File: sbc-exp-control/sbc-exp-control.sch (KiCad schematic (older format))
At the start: 10 parts, among them J1 P, SW1 U, SW2 D, SW3 L, SW4 R, SW5 A, SW6 B, SW7 C

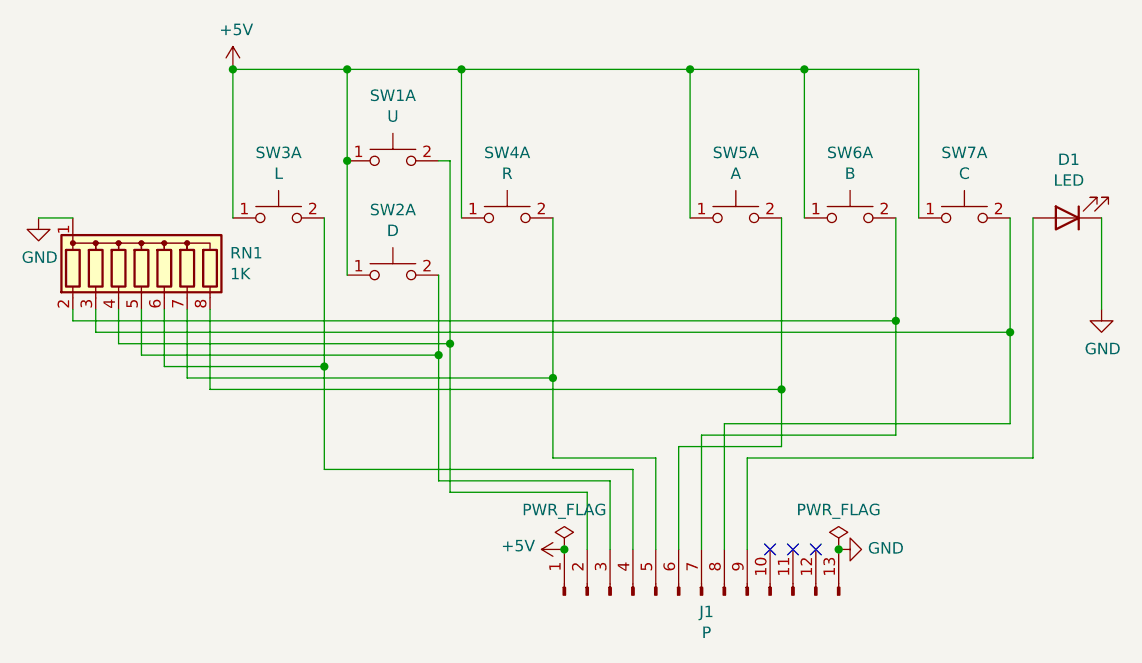
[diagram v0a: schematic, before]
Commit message: SBC Controller: Fix v1.0 errata
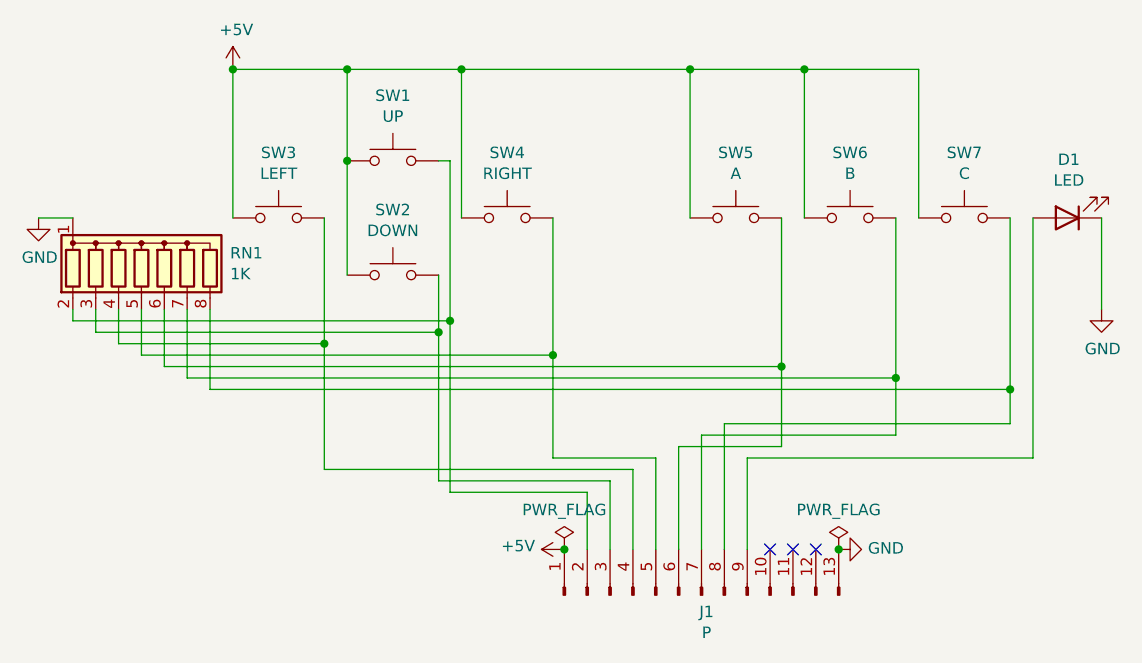
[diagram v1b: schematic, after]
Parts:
- removed SW1: U, switch:SW_TH_Tactile_Omron_B3F-10xx, symbol switch:SW_Push_Dual_x2
- removed SW2: D, switch:SW_TH_Tactile_Omron_B3F-10xx, symbol switch:SW_Push_Dual_x2
- removed SW3: L, switch:SW_TH_Tactile_Omron_B3F-10xx, symbol switch:SW_Push_Dual_x2
- removed SW4: R, switch:SW_TH_Tactile_Omron_B3F-10xx, symbol switch:SW_Push_Dual_x2
- removed SW5: A, switch:SW_TH_Tactile_Omron_B3F-10xx, symbol switch:SW_Push_Dual_x2
- removed SW6: B, switch:SW_TH_Tactile_Omron_B3F-10xx, symbol switch:SW_Push_Dual_x2
- removed SW7: C, switch:SW_TH_Tactile_Omron_B3F-10xx, symbol switch:SW_Push_Dual_x2
- added SW1: UP, switch:SW_TH_Tactile_Omron_B3F-10xx, symbol switch_tactile:SW_Tactile_Push
- added SW2: DOWN, switch:SW_TH_Tactile_Omron_B3F-10xx, symbol switch_tactile:SW_Tactile_Push
- added SW3: LEFT, switch:SW_TH_Tactile_Omron_B3F-10xx, symbol switch_tactile:SW_Tactile_Push
- added SW4: RIGHT, switch:SW_TH_Tactile_Omron_B3F-10xx, symbol switch_tactile:SW_Tactile_Push
- added SW5: A, switch:SW_TH_Tactile_Omron_B3F-10xx, symbol switch_tactile:SW_Tactile_Push
- added SW6: B, switch:SW_TH_Tactile_Omron_B3F-10xx, symbol switch_tactile:SW_Tactile_Push
- added SW7: C, switch:SW_TH_Tactile_Omron_B3F-10xx, symbol switch_tactile:SW_Tactile_Push
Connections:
- net +5V: now also SW1.1, SW2.1, SW3.1, SW4.1, SW5.1, SW6.1, SW7.1
- net at RN1.2 (R1): now also J1.2 (Pin_2), SW1.3; no longer J1.7 (Pin_7)
- net at RN1.3 (R2): now also J1.3 (Pin_3), SW2.3; no longer J1.8 (Pin_8)
- net at RN1.4 (R3): now also J1.4 (Pin_4), SW3.3; no longer J1.2 (Pin_2)
- net at RN1.5 (R4): now also J1.5 (Pin_5), SW4.3; no longer J1.3 (Pin_3)
- net at RN1.6 (R5): now also J1.6 (Pin_6), SW5.3; no longer J1.4 (Pin_4)
- net at RN1.7 (R6): now also J1.7 (Pin_7), SW6.3; no longer J1.5 (Pin_5)
- net at RN1.8 (R7): now also J1.8 (Pin_8), SW7.3; no longer J1.6 (Pin_6)
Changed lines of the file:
@@
 Sheet 1 1
 Title "6502 SBC Expansion - Controller"
-Date "2021-09-15"
-Rev "1.0"
+Date "2021-10-03"
+Rev "1.1"
 Comp ""
 Comment1 ""
@@
 	1    0    0    -1
 $EndComp
-$Comp
-L switch:SW_Push_Dual_x2 SW1
-U 1 1 6149A8C0
-P 4400 2900
-F 0 "SW1" H 4400 3185 50  0000 C CNN
-F 1 "U" H 4400 3094 50  0000 C CNN
-F 2 "switch:SW_TH_Tactile_Omron_B3F-10xx" H 4400 3100 50  0001 C CNN
-F 3 "~" H 4400 3100 50  0001 C CNN
-	1    4400 2900
-	1    0    0    -1
-$EndComp
-$Comp
-L switch:SW_Push_Dual_x2 SW2
-U 1 1 6149E1BC
-P 4400 3400
-F 0 "SW2" H 4400 3685 50  0000 C CNN
-F 1 "D" H 4400 3594 50  0000 C CNN
-F 2 "switch:SW_TH_Tactile_Omron_B3F-10xx" H 4400 3600 50  0001 C CNN
-F 3 "~" H 4400 3600 50  0001 C CNN
-	1    4400 3400
-	1    0    0    -1
-$EndComp
-$Comp
-L switch:SW_Push_Dual_x2 SW3
-U 1 1 6149E449
-P 3900 3150
-F 0 "SW3" H 3900 3435 50  0000 C CNN
-F 1 "L" H 3900 3344 50  0000 C CNN
-F 2 "switch:SW_TH_Tactile_Omron_B3F-10xx" H 3900 3350 50  0001 C CNN
-F 3 "~" H 3900 3350 50  0001 C CNN
-	1    3900 3150
-	1    0    0    -1
-$EndComp
-$Comp
-L switch:SW_Push_Dual_x2 SW4
-U 1 1 6149E6A4
-P 4900 3150
-F 0 "SW4" H 4900 3435 50  0000 C CNN
-F 1 "R" H 4900 3344 50  0000 C CNN
-F 2 "switch:SW_TH_Tactile_Omron_B3F-10xx" H 4900 3350 50  0001 C CNN
-F 3 "~" H 4900 3350 50  0001 C CNN
-	1    4900 3150
-	1    0    0    -1
-$EndComp
-$Comp
-L switch:SW_Push_Dual_x2 SW5
-U 1 1 6149E910
-P 5900 3150
-F 0 "SW5" H 5900 3435 50  0000 C CNN
-F 1 "A" H 5900 3344 50  0000 C CNN
-F 2 "switch:SW_TH_Tactile_Omron_B3F-10xx" H 5900 3350 50  0001 C CNN
-F 3 "~" H 5900 3350 50  0001 C CNN
-	1    5900 3150
-	1    0    0    -1
-$EndComp
-$Comp
-L switch:SW_Push_Dual_x2 SW6
-U 1 1 6149ECA4
-P 6400 3150
-F 0 "SW6" H 6400 3435 50  0000 C CNN
-F 1 "B" H 6400 3344 50  0000 C CNN
-F 2 "switch:SW_TH_Tactile_Omron_B3F-10xx" H 6400 3350 50  0001 C CNN
-F 3 "~" H 6400 3350 50  0001 C CNN
-	1    6400 3150
-	1    0    0    -1
-$EndComp
-$Comp
-L switch:SW_Push_Dual_x2 SW7
-U 1 1 6149EF8F
-P 6900 3150
-F 0 "SW7" H 6900 3435 50  0000 C CNN
-F 1 "C" H 6900 3344 50  0000 C CNN
-F 2 "switch:SW_TH_Tactile_Omron_B3F-10xx" H 6900 3350 50  0001 C CNN
-F 3 "~" H 6900 3350 50  0001 C CNN
-	1    6900 3150
-	1    0    0    -1
-$EndComp
 Wire Wire Line
 	4600 2900 4650 2900
-Wire Wire Line
-	4650 2900 4650 3700
-Wire Wire Line
-	4100 4250 4100 3800
-Wire Wire Line
-	5100 4200 5100 3850
-Wire Wire Line
-	6100 4150 6100 3900
 Wire Wire Line
 	3700 3150 3700 2500
@@
 Wire Wire Line
 	4700 2500 5700 2500
-Wire Wire Line
-	4200 2900 4200 2500
 Connection ~ 4200 2500
 Wire Wire Line
 	4200 2500 4700 2500
-Wire Wire Line
-	4200 3400 4200 2900
-Connection ~ 4200 2900
 $Comp
 L power:+5V #PWR0101
@@
 	3000 3550 3000 3600
 Wire Wire Line
-	3000 3600 6600 3600
-Wire Wire Line
-	6600 4100 6600 3600
-Wire Wire Line
-	6600 3600 6600 3150
-Connection ~ 6600 3600
-Wire Wire Line
 	3100 3550 3100 3650
 Wire Wire Line
-	3100 3650 7100 3650
-Wire Wire Line
-	7100 4050 7100 3650
-Wire Wire Line
-	7100 3650 7100 3150
-Connection ~ 7100 3650
-Wire Wire Line
-	4600 4300 4600 3750
-Wire Wire Line
 	3200 3550 3200 3700
 Wire Wire Line
-	3200 3700 4650 3700
-Connection ~ 4650 3700
-Wire Wire Line
-	4650 3700 4650 4350
-Wire Wire Line
 	3300 3550 3300 3750
 Wire Wire Line
-	3300 3750 4600 3750
-Connection ~ 4600 3750
-Wire Wire Line
-	4600 3750 4600 3400
-Wire Wire Line
 	3400 3550 3400 3800
 Wire Wire Line
-	3400 3800 4100 3800
-Connection ~ 4100 3800
-Wire Wire Line
-	4100 3800 4100 3150
-Wire Wire Line
 	3500 3550 3500 3850
 Wire Wire Line
-	3500 3850 5100 3850
-Connection ~ 5100 3850
-Wire Wire Line
-	5100 3850 5100 3150
-Wire Wire Line
 	3600 3550 3600 3900
-Wire Wire Line
-	3600 3900 6100 3900
-Connection ~ 6100 3900
-Wire Wire Line
-	6100 3900 6100 3150
-$Comp
-L power:GND #PWR?
+$Comp
+L power:GND #PWR0105
 U 1 1 6157BBDC
 P 2850 3150
-F 0 "#PWR?" H 2850 2900 50  0001 C CNN
+F 0 "#PWR0105" H 2850 2900 50  0001 C CNN
 F 1 "GND" H 2855 2977 50  0000 C CNN
 F 2 "" H 2850 3150 50  0001 C CNN
@@
 Wire Wire Line
 	2850 3150 3000 3150
+$Comp
+L switch_tactile:SW_Tactile_Push SW1
+U 1 1 615A9629
+P 4400 2900
+F 0 "SW1" H 4400 3185 50  0000 C CNN
+F 1 "UP" H 4400 3094 50  0000 C CNN
+F 2 "switch:SW_TH_Tactile_Omron_B3F-10xx" H 4400 3100 50  0001 C CNN
+F 3 "~" H 4400 3100 50  0001 C CNN
+	1    4400 2900
+	1    0    0    -1
+$EndComp
+$Comp
+L switch_tactile:SW_Tactile_Push SW2
+U 1 1 615A9B42
+P 4400 3400
+F 0 "SW2" H 4400 3685 50  0000 C CNN
+F 1 "DOWN" H 4400 3594 50  0000 C CNN
+F 2 "switch:SW_TH_Tactile_Omron_B3F-10xx" H 4400 3600 50  0001 C CNN
+F 3 "~" H 4400 3600 50  0001 C CNN
+	1    4400 3400
+	1    0    0    -1
+$EndComp
+$Comp
+L switch_tactile:SW_Tactile_Push SW3
+U 1 1 615A9FB0
+P 3900 3150
+F 0 "SW3" H 3900 3435 50  0000 C CNN
+F 1 "LEFT" H 3900 3344 50  0000 C CNN
+F 2 "switch:SW_TH_Tactile_Omron_B3F-10xx" H 3900 3350 50  0001 C CNN
+F 3 "~" H 3900 3350 50  0001 C CNN
+	1    3900 3150
+	1    0    0    -1
+$EndComp
+$Comp
+L switch_tactile:SW_Tactile_Push SW5
+U 1 1 615AABD4
+P 5900 3150
+F 0 "SW5" H 5900 3435 50  0000 C CNN
+F 1 "A" H 5900 3344 50  0000 C CNN
+F 2 "switch:SW_TH_Tactile_Omron_B3F-10xx" H 5900 3350 50  0001 C CNN
+F 3 "~" H 5900 3350 50  0001 C CNN
+	1    5900 3150
+	1    0    0    -1
+$EndComp
+$Comp
+L switch_tactile:SW_Tactile_Push SW6
+U 1 1 615AB121
+P 6400 3150
+F 0 "SW6" H 6400 3435 50  0000 C CNN
+F 1 "B" H 6400 3344 50  0000 C CNN
+F 2 "switch:SW_TH_Tactile_Omron_B3F-10xx" H 6400 3350 50  0001 C CNN
+F 3 "~" H 6400 3350 50  0001 C CNN
+	1    6400 3150
+	1    0    0    -1
+$EndComp
+$Comp
+L switch_tactile:SW_Tactile_Push SW7
+U 1 1 615AB5F9
+P 6900 3150
+F 0 "SW7" H 6900 3435 50  0000 C CNN
+F 1 "C" H 6900 3344 50  0000 C CNN
+F 2 "switch:SW_TH_Tactile_Omron_B3F-10xx" H 6900 3350 50  0001 C CNN
+F 3 "~" H 6900 3350 50  0001 C CNN
+	1    6900 3150
+	1    0    0    -1
+$EndComp
+Wire Wire Line
+	4200 2500 4200 2900
+Connection ~ 4200 2900
+Wire Wire Line
+	4200 2900 4200 3400
+$Comp
+L switch_tactile:SW_Tactile_Push SW4
+U 1 1 615AA694
+P 4900 3150
+F 0 "SW4" H 4900 3435 50  0000 C CNN
+F 1 "RIGHT" H 4900 3344 50  0000 C CNN
+F 2 "switch:SW_TH_Tactile_Omron_B3F-10xx" H 4900 3350 50  0001 C CNN
+F 3 "~" H 4900 3350 50  0001 C CNN
+	1    4900 3150
+	1    0    0    -1
+$EndComp
+Wire Wire Line
+	6600 3150 6600 3850
+Wire Wire Line
+	7100 3150 7100 3900
+Wire Wire Line
+	6100 3150 6100 3800
+Wire Wire Line
+	5100 3150 5100 3750
+Wire Wire Line
+	4600 3400 4600 3650
+Wire Wire Line
+	4100 3150 4100 3700
+Wire Wire Line
+	3000 3600 4650 3600
+Wire Wire Line
+	4650 2900 4650 3600
+Connection ~ 4650 3600
+Wire Wire Line
+	4650 3600 4650 4350
+Wire Wire Line
+	3100 3650 4600 3650
+Connection ~ 4600 3650
+Wire Wire Line
+	4600 3650 4600 4300
+Wire Wire Line
+	3200 3700 4100 3700
+Connection ~ 4100 3700
+Wire Wire Line
+	4100 3700 4100 4250
+Wire Wire Line
+	3300 3750 5100 3750
+Connection ~ 5100 3750
+Wire Wire Line
+	5100 3750 5100 4200
+Wire Wire Line
+	3400 3800 6100 3800
+Connection ~ 6100 3800
+Wire Wire Line
+	6100 3800 6100 4150
+Wire Wire Line
+	3500 3850 6600 3850
+Connection ~ 6600 3850
+Wire Wire Line
+	6600 3850 6600 4100
+Wire Wire Line
+	3600 3900 7100 3900
+Connection ~ 7100 3900
+Wire Wire Line
+	7100 3900 7100 4050
 $EndSCHEMATC

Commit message: SBC v2.0
Changes:

 - Second VIA
 - NMI button (hardware debounced)
 - 5 status LEDs (power and each VIA port)
 - Ground and power planes
 - Smaller footprint RAM and oscillator
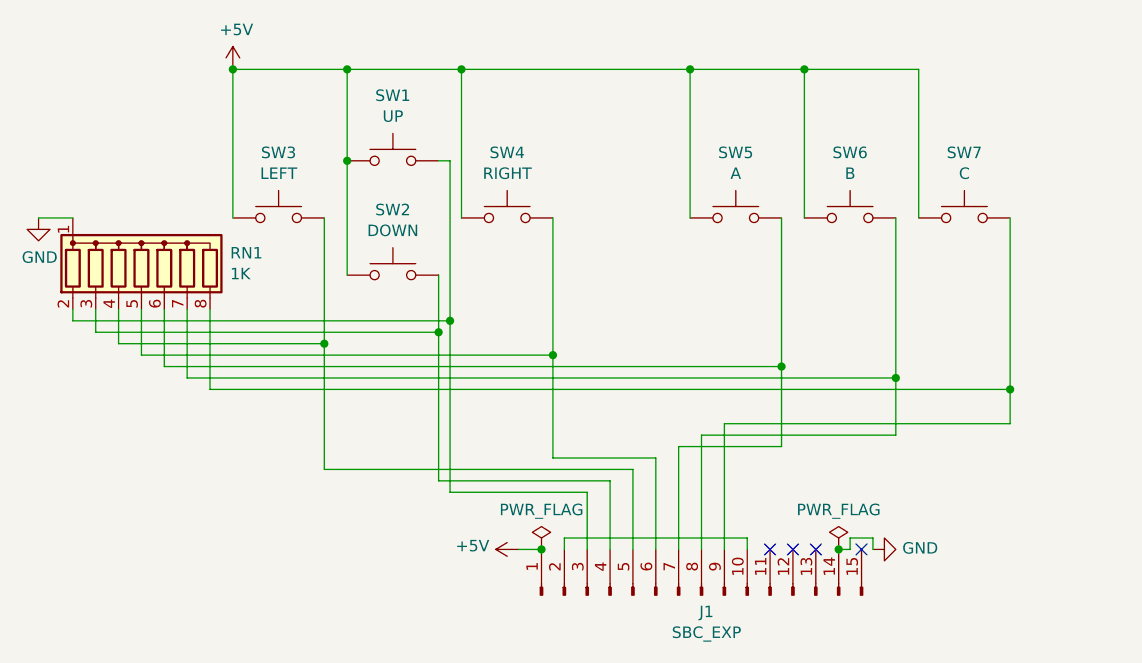
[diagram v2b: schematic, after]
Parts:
- removed D1: LED, led:LED_D5.0mm, symbol device:LED
- removed J1: P, connector:PinHeader_1x13_P2.54mm_Vertical, symbol connector:Conn_01x13_Male
- added J1: SBC_EXP, connector:PinHeader_1x15_P2.54mm_Vertical, symbol connector:Conn_01x15_Male
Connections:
- net +5V: now also J1.1 (Pin_1)
- net GND: now also J1.14 (Pin_14)
- net at RN1.2 (R1), SW1.3: now also J1.3 (Pin_3)
- net at RN1.3 (R2), SW2.3: now also J1.4 (Pin_4)
- net at RN1.4 (R3), SW3.3: now also J1.5 (Pin_5)
- net at RN1.5 (R4), SW4.3: now also J1.6 (Pin_6)
- net at RN1.6 (R5), SW5.3: now also J1.7 (Pin_7)
- net at RN1.7 (R6), SW6.3: now also J1.8 (Pin_8)
- net at RN1.8 (R7), SW7.3: now also J1.9 (Pin_9)
- new net: J1.10 (Pin_10), J1.2 (Pin_2)
- no-connect marks 3 -> 4
